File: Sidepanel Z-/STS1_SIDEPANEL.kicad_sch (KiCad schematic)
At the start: 5 parts, among them J1 Conn_01x08, J3 Conn_02x02_Odd_Even

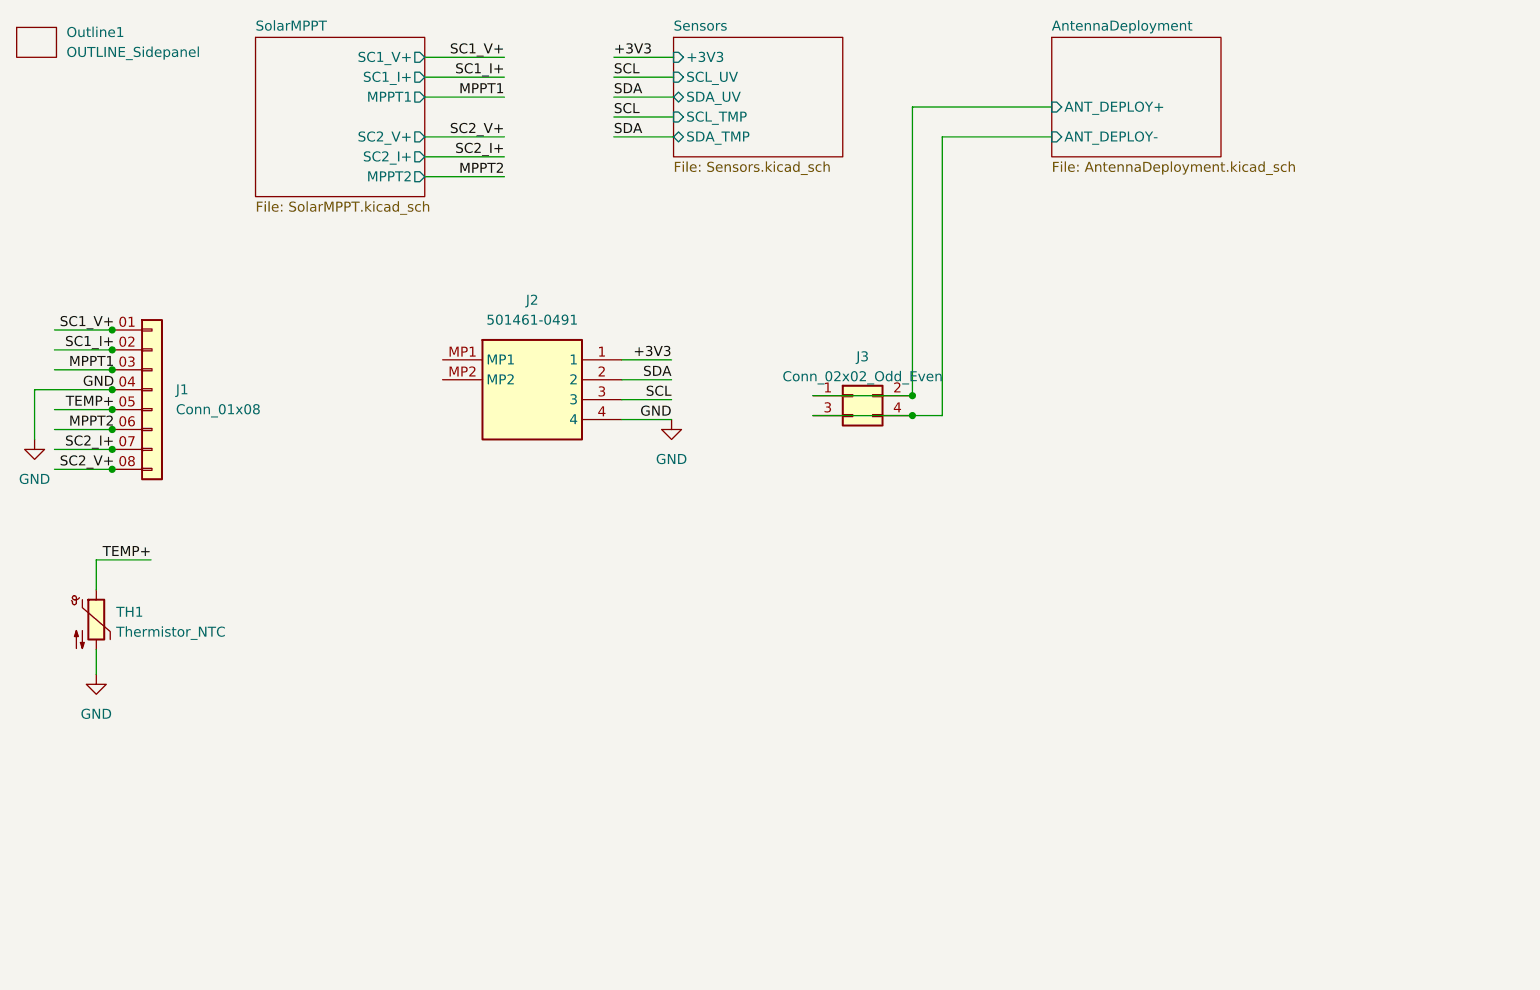
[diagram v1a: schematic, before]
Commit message: Changed the layout of all the sidepanel PCBs to mitigate the problems that arised from the bad previous design.
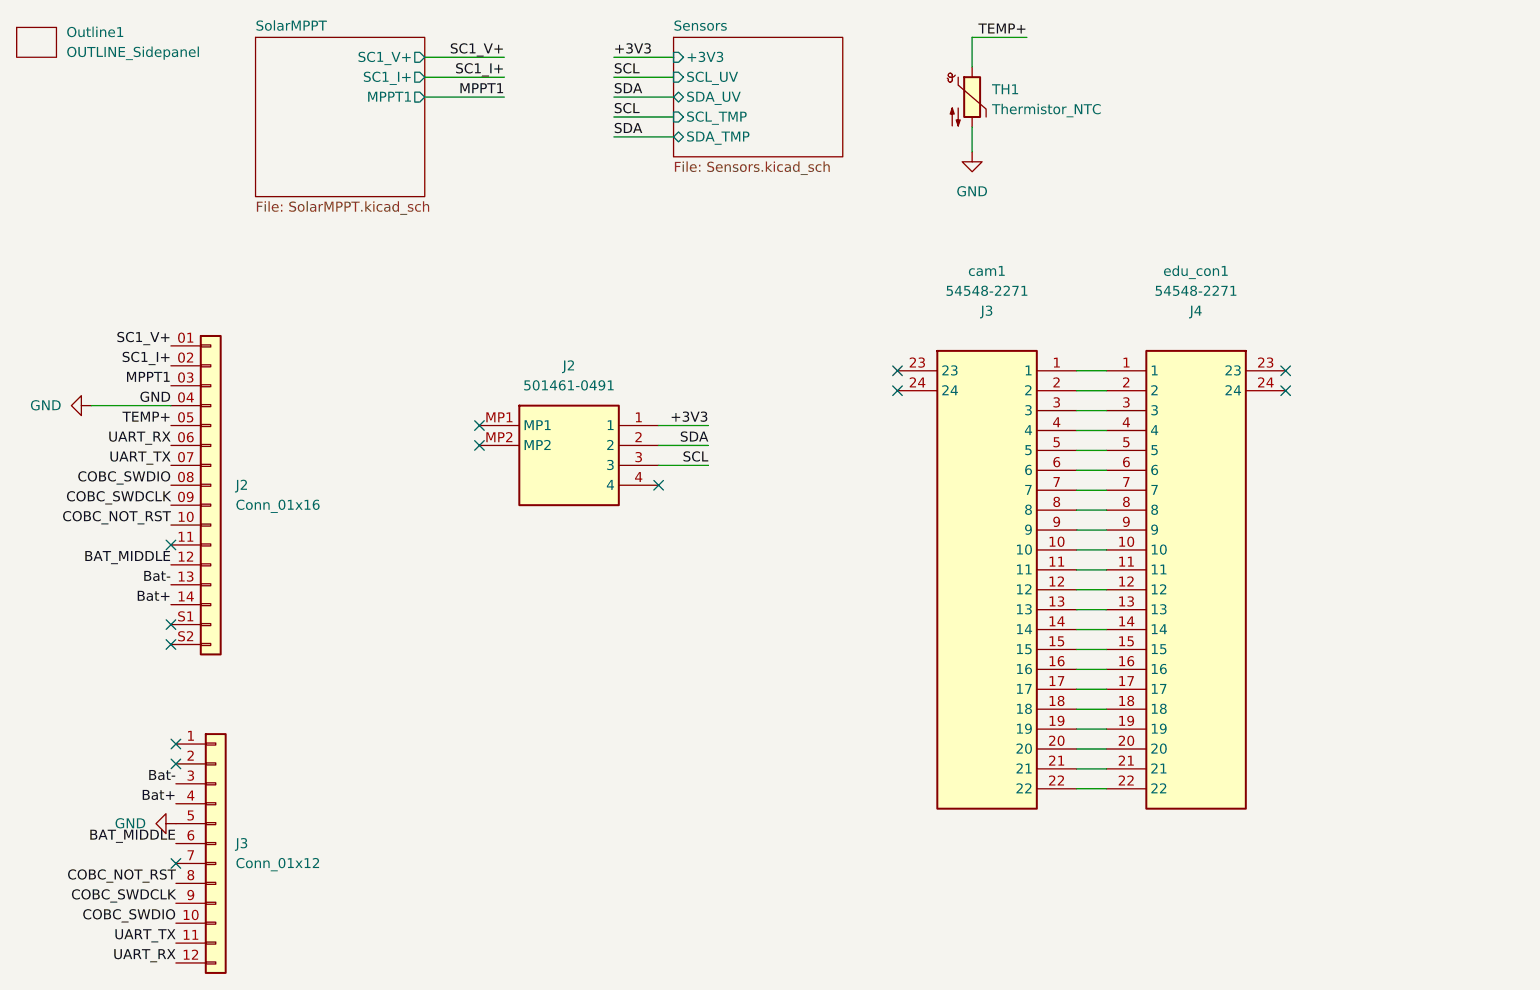
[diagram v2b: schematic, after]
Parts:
- removed J1: Conn_01x08, STS_Connector:SAMTEC_ZF5S-08-01-T-WT, symbol Connector_Generic:Conn_01x08
- removed J3: Conn_02x02_Odd_Even, STS_Connector:M808280442, symbol Connector_Generic:Conn_02x02_Odd_Even
- added J2: Conn_01x16, STS_connector:SAMTEC_ZF5S-14-01-T-WT, symbol Connector_Generic:Conn_01x16
- added J3: Conn_01x12, STS_connector:conn_to_panel, symbol Connector_Generic:Conn_01x12
- added cam1, edu_con1: 54548-2271, STS_connector:545482271, symbol Cam:54548-2271
- Outline1: footprint USER_OUTLINE:OUTLINE_SidepanelZ+ -> STS_Sidepanels_Outline:OUTLINE_SidepanelZ-
- UV1: footprint STS_Connector:5014610491 -> STS_connector:5014610491
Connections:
- net GND: now also J2.04 (Pin_4), J3.5 (Pin_5); no longer UV1.4
- net MPPT1: now also J2.03 (Pin_3)
- net SC1_I+: now also J2.02 (Pin_2)
- net SC1_V+: now also J2.01 (Pin_1)
- net TEMP+: now also J2.05 (Pin_5)
- new net: cam1.1, edu_con1.1
- new net: cam1.10, edu_con1.10
- new net: cam1.11, edu_con1.11
- new net: cam1.12, edu_con1.12
- new net: cam1.13, edu_con1.13
- new net: cam1.14, edu_con1.14
- new net: cam1.15, edu_con1.15
- new net: cam1.16, edu_con1.16
- new net: cam1.17, edu_con1.17
- new net: cam1.18, edu_con1.18
- new net: cam1.19, edu_con1.19
- new net: cam1.2, edu_con1.2
- new net: cam1.20, edu_con1.20
- new net: cam1.21, edu_con1.21
- new net: cam1.22, edu_con1.22
- new net: cam1.3, edu_con1.3
- new net: cam1.4, edu_con1.4
- new net: cam1.5, edu_con1.5
- new net: cam1.6, edu_con1.6
- new net: cam1.7, edu_con1.7
- new net: cam1.8, edu_con1.8
- new net: cam1.9, edu_con1.9
- new net BAT_MIDDLE: J2.12 (Pin_12), J3.6 (Pin_6)
- new net Bat+: J2.14 (Pin_14), J3.4 (Pin_4)
- new net Bat-: J2.13 (Pin_13), J3.3 (Pin_3)
- new net COBC_NOT_RST: J2.10 (Pin_10), J3.8 (Pin_8)
- new net COBC_SWDCLK: J2.09 (Pin_9), J3.9 (Pin_9)
- new net COBC_SWDIO: J2.08 (Pin_8), J3.10 (Pin_10)
- new net UART_RX: J2.06 (Pin_6), J3.12 (Pin_12)
- new net UART_TX: J2.07 (Pin_7), J3.11 (Pin_11)
- no-connect marks 0 -> 13
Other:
- removed sheet AntennaDeployment
- sheet SolarMPPT ports: added none; removed MPPT2, SC2_I+, SC2_V+

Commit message: Added a  separate ground for the EDU  sensors and did  some small changes for ordering.
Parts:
- removed J2: Conn_01x16, STS_connector:SAMTEC_ZF5S-14-01-T-WT, symbol Connector_Generic:Conn_01x16
- added J1: Conn_01x18, STS_connector:SAMTEC_ZF5S-16-01-T-WT, symbol Connector_Generic:Conn_01x18
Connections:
- net BAT_MIDDLE is gone; now on net GND: J3.6 (Pin_6)
- net Bat+: now also J1.15 (Pin_15), J1.16 (Pin_16)
- net Bat-: now also J1.13 (Pin_13), J1.14 (Pin_14)
- net COBC_NOT_RST: now also J3.10 (Pin_10), J1.08 (Pin_8); no longer J3.8 (Pin_8)
- net COBC_SWDCLK: now also J3.8 (Pin_8), J1.10 (Pin_10); no longer J3.9 (Pin_9)
- net COBC_SWDIO: now also J3.9 (Pin_9), J1.09 (Pin_9); no longer J3.10 (Pin_10)
- net GND: now also J3.7 (Pin_7), J1.04 (Pin_4); no longer J3.5 (Pin_5)
- net MPPT1: now also J1.03 (Pin_3)
- net SC1_I+: now also J1.02 (Pin_2)
- net SC1_V+: now also J1.01 (Pin_1)
- net TEMP+: now also J1.05 (Pin_5)
- net UART_RX: now also J1.06 (Pin_6)
- net UART_TX: now also J1.07 (Pin_7)
- net GND1: now reaches UV1.4
- new net +5V: J1.11 (Pin_11), J3.5 (Pin_5)
- no-connect marks 13 -> 11
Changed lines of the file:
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@@
 (kicad_sch (version 20230121) (generator eeschema)
   (paper "A4")
-  (no_connect (at 102.235 83.82))
-  (no_connect (at 40.005 91.44))
-  (no_connect (at 40.005 101.6))
+  (no_connect (at 40.64 116.84))
   (no_connect (at 79.375 76.2))
+  (no_connect (at 40.005 93.98))
   (no_connect (at 132.715 71.755))
-  (no_connect (at 40.64 116.84))
+  (no_connect (at 40.64 119.38))
   (no_connect (at 182.245 71.755))
-  (no_connect (at 40.64 119.38))
+  (no_connect (at 40.005 109.22))
   (no_connect (at 79.375 78.74))
   (no_connect (at 182.245 69.215))
-  (no_connect (at 40.005 104.14))
-  (no_connect (at 40.64 132.08))
   (no_connect (at 132.715 69.215))
+  (no_connect (at 40.005 106.68))
   (wire (pts (xy 155.575 109.855) (xy 159.385 109.855))
     (stroke (width 0) (type default))
@@
     (effects (font (size 1.27 1.27)) (justify right bottom))
   )
-  (label "COBC_SWDIO" (at 40.005 83.82 180) (fields_autoplaced)
+  (label "COBC_SWDIO" (at 40.005 86.36 180) (fields_autoplaced)
     (effects (font (size 1.27 1.27)) (justify right bottom))
   )
@@
     (effects (font (size 1.27 1.27)) (justify right bottom))
   )
-  (label "BAT_MIDDLE" (at 40.005 93.98 180) (fields_autoplaced)
-    (effects (font (size 1.27 1.27)) (justify right bottom))
-  )
-  (label "COBC_SWDCLK" (at 40.64 137.16 180) (fields_autoplaced)
+  (label "COBC_SWDCLK" (at 40.64 134.62 180) (fields_autoplaced)
     (effects (font (size 1.27 1.27)) (justify right bottom))
   )
@@
     (effects (font (size 1.27 1.27)) (justify right bottom))
   )
-  (label "Bat+" (at 40.005 99.06 180) (fields_autoplaced)
+  (label "Bat+" (at 40.005 104.14 180) (fields_autoplaced)
     (effects (font (size 1.27 1.27)) (justify right bottom))
   )
@@
     (effects (font (size 1.27 1.27)) (justify right bottom))
   )
-  (label "COBC_SWDCLK" (at 40.005 86.36 180) (fields_autoplaced)
-    (effects (font (size 1.27 1.27)) (justify right bottom))
-  )
-  (label "COBC_NOT_RST" (at 40.64 134.62 180) (fields_autoplaced)
+  (label "COBC_SWDCLK" (at 40.005 88.9 180) (fields_autoplaced)
+    (effects (font (size 1.27 1.27)) (justify right bottom))
+  )
+  (label "COBC_NOT_RST" (at 40.64 139.7 180) (fields_autoplaced)
+    (effects (font (size 1.27 1.27)) (justify right bottom))
+  )
+  (label "Bat-" (at 40.005 99.06 180) (fields_autoplaced)
     (effects (font (size 1.27 1.27)) (justify right bottom))
   )
@@
     (effects (font (size 1.27 1.27)) (justify right bottom))
   )
+  (label "Bat+" (at 40.005 101.6 180) (fields_autoplaced)
+    (effects (font (size 1.27 1.27)) (justify right bottom))
+  )
   (label "Bat-" (at 40.64 121.92 180) (fields_autoplaced)
     (effects (font (size 1.27 1.27)) (justify right bottom))
   )
-  (label "BAT_MIDDLE" (at 40.64 129.54 180) (fields_autoplaced)
-    (effects (font (size 1.27 1.27)) (justify right bottom))
-  )
   (label "+3V3" (at 108.585 76.2 180) (fields_autoplaced)
     (effects (font (size 1.27 1.27)) (justify right bottom))
@@
     (effects (font (size 1.27 1.27)) (justify right bottom))
   )
-  (label "COBC_NOT_RST" (at 40.005 88.9 180) (fields_autoplaced)
+  (label "COBC_NOT_RST" (at 40.005 83.82 180) (fields_autoplaced)
     (effects (font (size 1.27 1.27)) (justify right bottom))
   )
@@
     (effects (font (size 1.27 1.27)) (justify right bottom))
   )
-  (label "COBC_SWDIO" (at 40.64 139.7 180) (fields_autoplaced)
+  (label "COBC_SWDIO" (at 40.64 137.16 180) (fields_autoplaced)
     (effects (font (size 1.27 1.27)) (justify right bottom))
   )
@@
     )
   )
+  (symbol (lib_id "power:GND1") (at 102.235 83.82 90) (unit 1)
+    (in_bom yes) (on_board yes) (dnp no) (fields_autoplaced)
+    (property "Reference" "#PWR07" (at 108.585 83.82 0)
+      (effects (font (size 1.27 1.27)) hide)
+    )
+    (property "Value" "GND1" (at 105.41 83.82 90)
+      (effects (font (size 1.27 1.27)) (justify right))
+    )
+    (property "Footprint" "" (at 102.235 83.82 0)
+      (effects (font (size 1.27 1.27)) hide)
+    )
+    (property "Datasheet" "" (at 102.235 83.82 0)
+      (effects (font (size 1.27 1.27)) hide)
+    )
+    (pin "1")
+    (instances
+      (project "STS1_SIDEPANEL"
+        (path "/e63e39d7-6ac0-4ffd-8aa3-1841a4541b55"
+          (reference "#PWR07") (unit 1)
+        )
+      )
+    )
+  )
   (symbol (lib_id "power:GND") (at 29.845 73.66 270) (unit 1)
     (in_bom yes) (on_board yes) (dnp no) (fields_autoplaced)
@@
     )
   )
-  (symbol (lib_id "power:GND") (at 40.64 127 270) (unit 1)
-    (in_bom yes) (on_board yes) (dnp no) (fields_autoplaced)
-    (property "Reference" "#PWR01" (at 34.29 127 0)
-      (effects (font (size 1.27 1.27)) hide)
-    )
-    (property "Value" "GND" (at 36.83 126.9999 90)
+  (symbol (lib_id "power:GND") (at 40.64 129.54 270) (unit 1)
+    (in_bom yes) (on_board yes) (dnp no) (fields_autoplaced)
+    (property "Reference" "#PWR01" (at 34.29 129.54 0)
+      (effects (font (size 1.27 1.27)) hide)
+    )
+    (property "Value" "GND" (at 36.83 129.5399 90)
       (effects (font (size 1.27 1.27)) (justify right))
     )
-    (property "Footprint" "" (at 40.64 127 0)
-      (effects (font (size 1.27 1.27)) hide)
-    )
-    (property "Datasheet" "" (at 40.64 127 0)
+    (property "Footprint" "" (at 40.64 129.54 0)
+      (effects (font (size 1.27 1.27)) hide)
+    )
+    (property "Datasheet" "" (at 40.64 129.54 0)
       (effects (font (size 1.27 1.27)) hide)
     )
@@
     )
   )
-  (symbol (lib_id "Connector_Generic:Conn_01x16") (at 45.085 83.82 0) (unit 1)
-    (in_bom yes) (on_board yes) (dnp no) (fields_autoplaced)
-    (property "Reference" "J2" (at 48.26 83.82 0)
-      (effects (font (size 1.27 1.27)) (justify left))
-    )
-    (property "Value" "Conn_01x16" (at 48.26 86.36 0)
-      (effects (font (size 1.27 1.27)) (justify left))
-    )
-    (property "Footprint" "STS_connector:SAMTEC_ZF5S-14-01-T-WT" (at 45.085 83.82 0)
-      (effects (font (size 1.27 1.27)) hide)
-    )
-    (property "Datasheet" "~" (at 45.085 83.82 0)
-      (effects (font (size 1.27 1.27)) hide)
-    )
-    (pin "06")
-    (pin "14")
-    (pin "S2")
-    (pin "11")
-    (pin "02")
-    (pin "10")
-    (pin "01")
-    (pin "05")
-    (pin "03")
-    (pin "09")
-    (pin "04")
-    (pin "07")
-    (pin "S1")
-    (pin "13")
-    (pin "12")
-    (pin "08")
-    (instances
-      (project "STS1_SIDEPANEL"
-        (path "/e63e39d7-6ac0-4ffd-8aa3-1841a4541b55"
-          (reference "J2") (unit 1)
+  (symbol (lib_id "power:GND") (at 40.64 132.08 270) (unit 1)
+    (in_bom yes) (on_board yes) (dnp no) (fields_autoplaced)
+    (property "Reference" "#PWR06" (at 34.29 132.08 0)
+      (effects (font (size 1.27 1.27)) hide)
+    )
+    (property "Value" "GND" (at 36.83 132.0799 90)
+      (effects (font (size 1.27 1.27)) (justify right))
+    )
+    (property "Footprint" "" (at 40.64 132.08 0)
+      (effects (font (size 1.27 1.27)) hide)
+    )
+    (property "Datasheet" "" (at 40.64 132.08 0)
+      (effects (font (size 1.27 1.27)) hide)
+    )
+    (pin "1")
+    (instances
+      (project "STS1_SIDEPANEL"
+        (path "/e63e39d7-6ac0-4ffd-8aa3-1841a4541b55"
+          (reference "#PWR06") (unit 1)
         )
       )
@@
     )
   )
+  (symbol (lib_id "power:+5V") (at 40.64 127 90) (unit 1)
+    (in_bom yes) (on_board yes) (dnp no) (fields_autoplaced)
+    (property "Reference" "#PWR05" (at 44.45 127 0)
+      (effects (font (size 1.27 1.27)) hide)
+    )
+    (property "Value" "+5V" (at 36.83 127 90)
+      (effects (font (size 1.27 1.27)) (justify left))
+    )
+    (property "Footprint" "" (at 40.64 127 0)
+      (effects (font (size 1.27 1.27)) hide)
+    )
+    (property "Datasheet" "" (at 40.64 127 0)
+      (effects (font (size 1.27 1.27)) hide)
+    )
+    (pin "1")
+    (instances
+      (project "STS1_SIDEPANEL"
+        (path "/e63e39d7-6ac0-4ffd-8aa3-1841a4541b55"
+          (reference "#PWR05") (unit 1)
+        )
+      )
+    )
+  )
+  (symbol (lib_id "power:+5V") (at 40.005 91.44 90) (unit 1)
+    (in_bom yes) (on_board yes) (dnp no) (fields_autoplaced)
+    (property "Reference" "#PWR08" (at 43.815 91.44 0)
+      (effects (font (size 1.27 1.27)) hide)
+    )
+    (property "Value" "+5V" (at 36.195 91.44 90)
+      (effects (font (size 1.27 1.27)) (justify left))
+    )
+    (property "Footprint" "" (at 40.005 91.44 0)
+      (effects (font (size 1.27 1.27)) hide)
+    )
+    (property "Datasheet" "" (at 40.005 91.44 0)
+      (effects (font (size 1.27 1.27)) hide)
+    )
+    (pin "1")
+    (instances
+      (project "STS1_SIDEPANEL"
+        (path "/e63e39d7-6ac0-4ffd-8aa3-1841a4541b55"
+          (reference "#PWR08") (unit 1)
+        )
+      )
+    )
+  )
   (symbol (lib_id "Cam:54548-2271") (at 182.245 69.215 0) (mirror y) (unit 1)
     (in_bom yes) (on_board yes) (dnp no) (fields_autoplaced)
@@
         )
       )
+    )
+  )
+  (symbol (lib_id "Connector_Generic:Conn_01x18") (at 45.085 86.36 0) (unit 1)
+    (in_bom yes) (on_board yes) (dnp no) (fields_autoplaced)
+    (property "Reference" "J1" (at 47.625 86.36 0)
+      (effects (font (size 1.27 1.27)) (justify left))
+    )
+    (property "Value" "Conn_01x18" (at 47.625 88.9 0)
+      (effects (font (size 1.27 1.27)) (justify left))
+    )
+    (property "Footprint" "STS_connector:SAMTEC_ZF5S-16-01-T-WT" (at 45.085 86.36 0)
+      (effects (font (size 1.27 1.27)) hide)
+    )
+    (property "Datasheet" "~" (at 45.085 86.36 0)
+      (effects (font (size 1.27 1.27)) hide)
+    )
+    (pin "05")
+    (pin "06")
+    (pin "02")
+    (pin "10")
+    (pin "15")
+    (pin "13")
+    (pin "12")
+    (pin "09")
+    (pin "07")
+    (pin "14")
+    (pin "03")
+    (pin "11")
+    (pin "S2")
+    (pin "04")
+    (pin "S1")
+    (pin "01")
+    (pin "08")
+    (pin "16")
+    (instances
+      (project "STS1_SIDEPANEL"
+        (path "/e63e39d7-6ac0-4ffd-8aa3-1841a4541b55"
+          (reference "J1") (unit 1)
+        )
+      )
